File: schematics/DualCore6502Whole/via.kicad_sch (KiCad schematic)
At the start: 4 parts, among them J3 PORTA/PORTB, U15 W65C22N

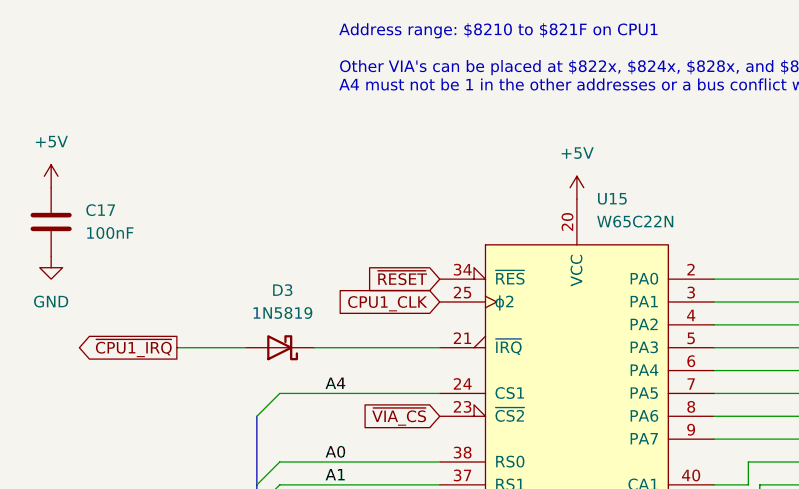
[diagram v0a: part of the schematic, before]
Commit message: Remove the need to multiplex the control lines
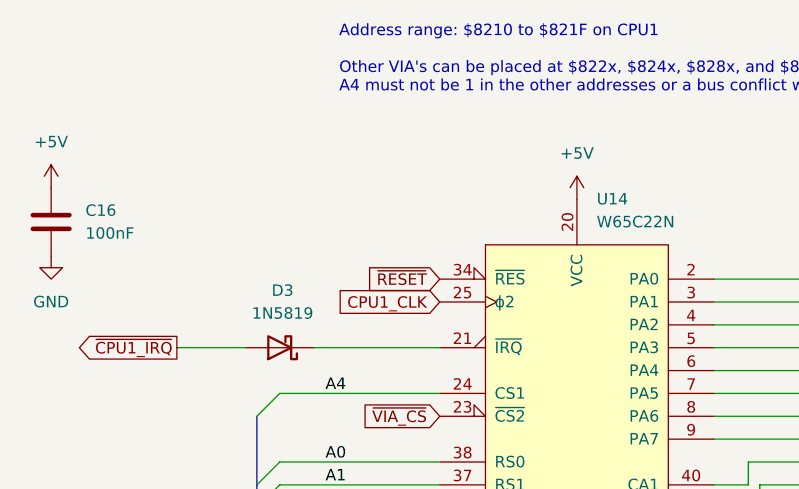
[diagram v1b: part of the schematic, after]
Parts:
- renumbered C17 to C16, U15 to U14
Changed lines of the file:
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@@
 		(dnp no)
 		(fields_autoplaced yes)
-		(property "Reference" "#PWR86"
+		(property "Reference" "#PWR79"
 			(at 78.74 59.69 0)
 			(effects
@@
 			(project "DualCore6502Whole"
 				(path "/93e0914e-b2e9-49c2-95f2-7cc419f4ea20/1a8142fa-4025-476a-8951-987d5052a061"
-					(reference "#PWR86")
+					(reference "#PWR79")
 					(unit 1)
 				)
@@
 		(dnp no)
 		(fields_autoplaced yes)
-		(property "Reference" "#PWR89"
+		(property "Reference" "#PWR82"
 			(at 137.16 137.16 0)
 			(effects
@@
 			(project ""
 				(path "/93e0914e-b2e9-49c2-95f2-7cc419f4ea20/1a8142fa-4025-476a-8951-987d5052a061"
-					(reference "#PWR89")
+					(reference "#PWR82")
 					(unit 1)
 				)
@@
 		(dnp no)
 		(fields_autoplaced yes)
-		(property "Reference" "#PWR88"
+		(property "Reference" "#PWR81"
 			(at 137.16 60.96 0)
 			(effects
@@
 			(project ""
 				(path "/93e0914e-b2e9-49c2-95f2-7cc419f4ea20/1a8142fa-4025-476a-8951-987d5052a061"
-					(reference "#PWR88")
+					(reference "#PWR81")
 					(unit 1)
 				)
@@
 		(dnp no)
 		(fields_autoplaced yes)
-		(property "Reference" "#PWR91"
+		(property "Reference" "#PWR84"
 			(at 165.1 93.98 0)
 			(effects
@@
 			(project "DualCore6502Whole"
 				(path "/93e0914e-b2e9-49c2-95f2-7cc419f4ea20/1a8142fa-4025-476a-8951-987d5052a061"
-					(reference "#PWR91")
+					(reference "#PWR84")
 					(unit 1)
 				)
@@
 		(dnp no)
 		(fields_autoplaced yes)
-		(property "Reference" "C17"
+		(property "Reference" "C16"
 			(at 82.55 58.42 0)
 			(effects
@@
 			(project "DualCore6502Whole"
 				(path "/93e0914e-b2e9-49c2-95f2-7cc419f4ea20/1a8142fa-4025-476a-8951-987d5052a061"
-					(reference "C17")
+					(reference "C16")
 					(unit 1)
 				)
@@
 		(dnp no)
 		(fields_autoplaced yes)
-		(property "Reference" "#PWR87"
+		(property "Reference" "#PWR80"
 			(at 78.74 69.85 0)
 			(effects
@@
 			(project "DualCore6502Whole"
 				(path "/93e0914e-b2e9-49c2-95f2-7cc419f4ea20/1a8142fa-4025-476a-8951-987d5052a061"
-					(reference "#PWR87")
+					(reference "#PWR80")
 					(unit 1)
 				)
@@
 		(dnp no)
 		(fields_autoplaced yes)
-		(property "Reference" "U15"
+		(property "Reference" "U14"
 			(at 139.3541 57.15 0)
 			(effects
@@
 			(project ""
 				(path "/93e0914e-b2e9-49c2-95f2-7cc419f4ea20/1a8142fa-4025-476a-8951-987d5052a061"
-					(reference "U15")
+					(reference "U14")
 					(unit 1)
 				)
@@
 		(dnp no)
 		(fields_autoplaced yes)
-		(property "Reference" "#PWR90"
+		(property "Reference" "#PWR83"
 			(at 175.26 91.44 0)
 			(effects
@@
 			(project "DualCore6502Whole"
 				(path "/93e0914e-b2e9-49c2-95f2-7cc419f4ea20/1a8142fa-4025-476a-8951-987d5052a061"
-					(reference "#PWR90")
-					(unit 1)
-				)
+					(reference "#PWR83")
+					(unit 1)
+				)

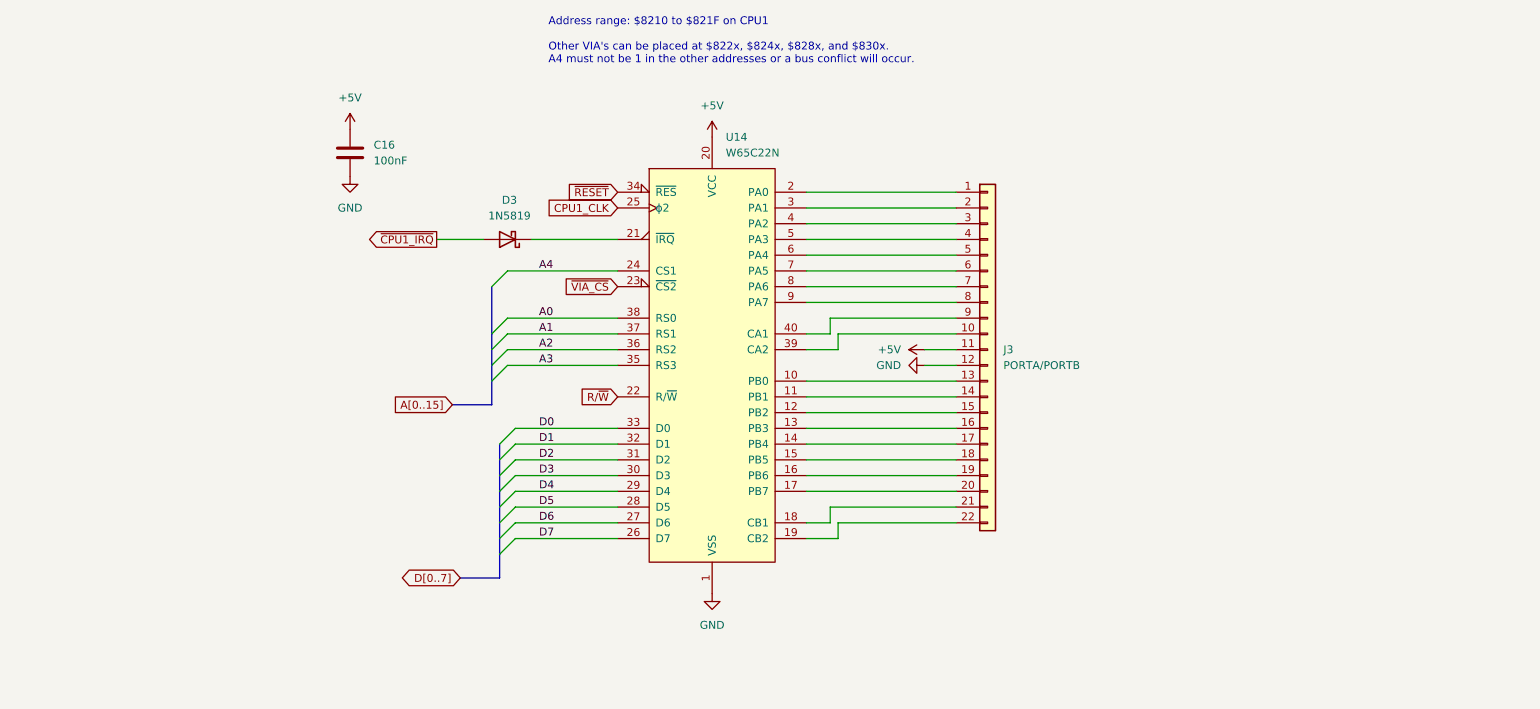
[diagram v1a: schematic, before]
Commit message: Add simpler I/O outputs as an alternative to the VIA
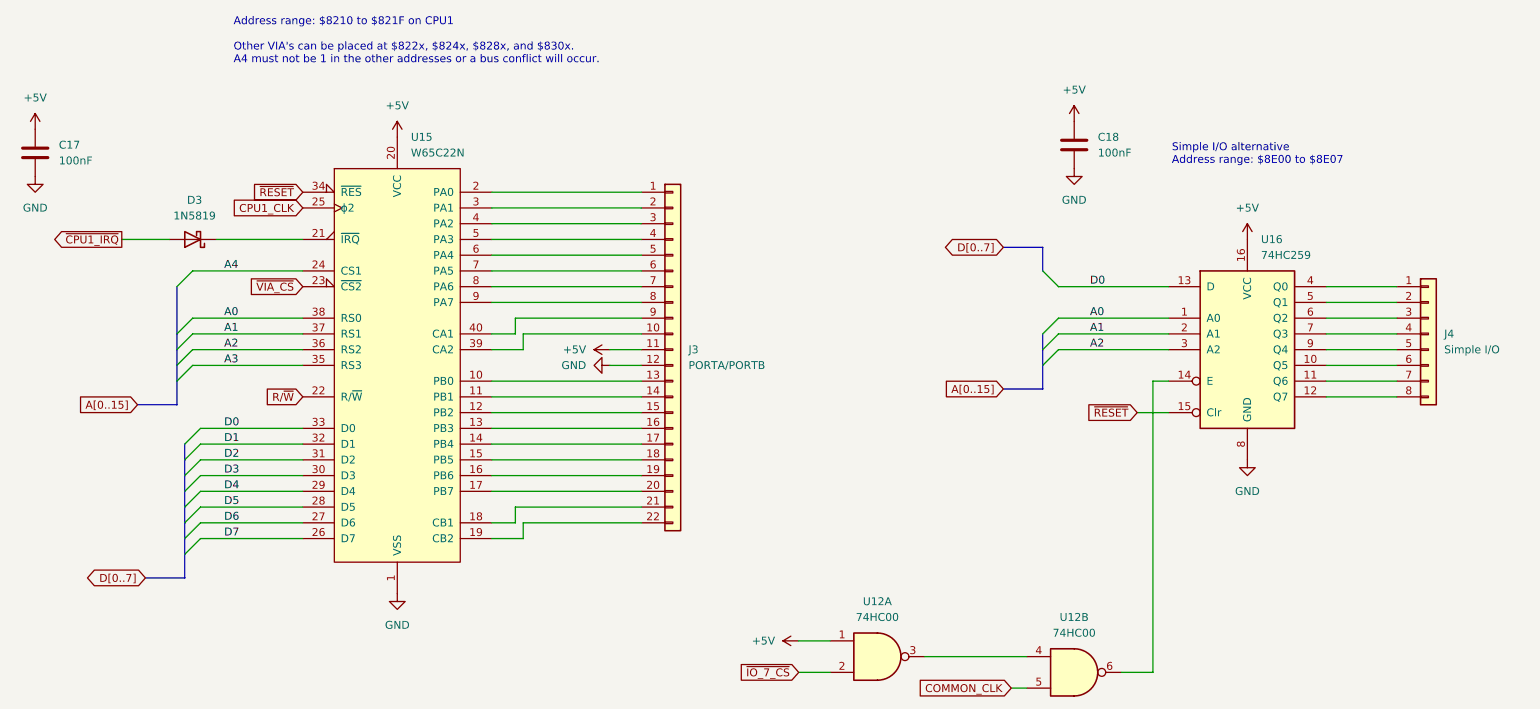
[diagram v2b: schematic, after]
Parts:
- added C18: 100nF, Capacitor_THT:C_Disc_D5.0mm_W2.5mm_P5.00mm, symbol Device:C
- added J4: Simple I/O, Connector_PinHeader_2.54mm:PinHeader_1x08_P2.54mm_Vertical, symbol Connector_Generic:Conn_01x08
- added U12: 74HC00, Package_DIP:DIP-14_W7.62mm, symbol 74xx:74LS00
- added U16: 74HC259, Package_DIP:DIP-16_W7.62mm, symbol 74xx:74LS259
- renumbered C16 to C17, U14 to U15
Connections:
- net +5V: now also C18.1, U12.1, U16.16 (VCC)
- net A0: now also U16.1 (A0)
- net A1: now also U16.2 (A1)
- net A2: now also U16.3 (A2)
- net D0: now also U16.13 (D)
- net GND: now also C18.2, U16.8 (GND)
- net ~{RESET}: now also U16.15 (Clr)
- new net: U12.3, U12.4
- new net: U12.6, U16.14 (E)
- new net: J4.6 (Pin_6), U16.10 (Q5)
- new net: J4.7 (Pin_7), U16.11 (Q6)
- new net: J4.8 (Pin_8), U16.12 (Q7)
- new net: J4.1 (Pin_1), U16.4 (Q0)
- new net: J4.2 (Pin_2), U16.5 (Q1)
- new net: J4.3 (Pin_3), U16.6 (Q2)
- new net: J4.4 (Pin_4), U16.7 (Q3)
- new net: J4.5 (Pin_5), U16.9 (Q4)
- new net COMMON_CLK: U12.5
- new net ~{IO_7_CS}: U12.2
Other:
- note added: "Simple I/O alternative Address range: $8E00 to $8E07"
- moved on the sheet: C17, D3, J3, U15

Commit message: Update the schematic
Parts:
- removed C18: 100nF, Capacitor_THT:C_Disc_D5.0mm_W2.5mm_P5.00mm, symbol Device:C
- removed J4: Simple I/O, Connector_PinHeader_2.54mm:PinHeader_1x08_P2.54mm_Vertical, symbol Connector_Generic:Conn_01x08
- removed U12: 74HC00, Package_DIP:DIP-14_W7.62mm, symbol 74xx:74LS00
- removed U16: 74HC259, Package_DIP:DIP-16_W7.62mm, symbol 74xx:74LS259
- added JP1: VIA IRQ, Connector_PinHeader_2.54mm:PinHeader_1x03_P2.54mm_Vertical, symbol Jumper:Jumper_3_Bridged12
- renumbered C17 to C21, D3 to D8, J3 to J4, U15 to U19
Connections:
- net CPU1_CLK is gone; now on net COMMON_CLK: U19.25 (ϕ2)
- net ~{CPU1_IRQ}: now also JP1.1 (A); no longer D8.2 (A)
- new net: D8.2 (A), JP1.2 (C)
- new net ~{CPU2_IRQ}: JP1.3 (B)
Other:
- note removed: "Simple I/O alternative Address range: $8E00 to $8E07"
- title: (none) -> Dual Core 65C02 Computer
- moved on the sheet: C21, D8, J4, U19

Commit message: Basic PCB layout
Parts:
- U18: renamed from U19; footprint Package_DIP:DIP-40_W15.24mm -> Package_DIP:DIP-40_W15.24mm_Socket
- renumbered C21 to C20, D8 to D7
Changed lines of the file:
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@@
 		(dnp no)
 		(fields_autoplaced yes)
-		(property "Reference" "#PWR116"
+		(property "Reference" "#PWR112"
 			(at 85.09 64.77 0)
 			(effects
@@
 			(project "DualCore6502Whole"
 				(path "/93e0914e-b2e9-49c2-95f2-7cc419f4ea20/1a8142fa-4025-476a-8951-987d5052a061"
-					(reference "#PWR116")
+					(reference "#PWR112")
 					(unit 1)
 				)
@@
 		(dnp no)
 		(fields_autoplaced yes)
-		(property "Reference" "#PWR119"
+		(property "Reference" "#PWR115"
 			(at 143.51 142.24 0)
 			(effects
@@
 			(project ""
 				(path "/93e0914e-b2e9-49c2-95f2-7cc419f4ea20/1a8142fa-4025-476a-8951-987d5052a061"
-					(reference "#PWR119")
+					(reference "#PWR115")
 					(unit 1)
 				)
@@
 		(dnp no)
 		(fields_autoplaced yes)
-		(property "Reference" "#PWR118"
+		(property "Reference" "#PWR114"
 			(at 143.51 66.04 0)
 			(effects
@@
 			(project ""
 				(path "/93e0914e-b2e9-49c2-95f2-7cc419f4ea20/1a8142fa-4025-476a-8951-987d5052a061"
-					(reference "#PWR118")
+					(reference "#PWR114")
 					(unit 1)
 				)
@@
 		(dnp no)
 		(fields_autoplaced yes)
-		(property "Reference" "D8"
+		(property "Reference" "D7"
 			(at 106.9975 72.39 0)
 			(effects
@@
 			(project "DualCore6502Whole"
 				(path "/93e0914e-b2e9-49c2-95f2-7cc419f4ea20/1a8142fa-4025-476a-8951-987d5052a061"
-					(reference "D8")
+					(reference "D7")
 					(unit 1)
 				)
@@
 		(dnp no)
 		(fields_autoplaced yes)
-		(property "Reference" "#PWR121"
+		(property "Reference" "#PWR117"
 			(at 171.45 99.06 0)
 			(effects
@@
 			(project "DualCore6502Whole"
 				(path "/93e0914e-b2e9-49c2-95f2-7cc419f4ea20/1a8142fa-4025-476a-8951-987d5052a061"
-					(reference "#PWR121")
+					(reference "#PWR117")
 					(unit 1)
 				)
@@
 		(dnp no)
 		(fields_autoplaced yes)
-		(property "Reference" "C21"
+		(property "Reference" "C20"
 			(at 88.9 63.5 0)
 			(effects
@@
 			(project "DualCore6502Whole"
 				(path "/93e0914e-b2e9-49c2-95f2-7cc419f4ea20/1a8142fa-4025-476a-8951-987d5052a061"
-					(reference "C21")
+					(reference "C20")
 					(unit 1)
 				)
@@
 		(dnp no)
 		(fields_autoplaced yes)
-		(property "Reference" "#PWR117"
+		(property "Reference" "#PWR113"
 			(at 85.09 74.93 0)
 			(effects
@@
 			(project "DualCore6502Whole"
 				(path "/93e0914e-b2e9-49c2-95f2-7cc419f4ea20/1a8142fa-4025-476a-8951-987d5052a061"
-					(reference "#PWR117")
+					(reference "#PWR113")
 					(unit 1)
 				)
@@
 		(dnp no)
 		(fields_autoplaced yes)
-		(property "Reference" "U19"
+		(property "Reference" "U18"
 			(at 145.7041 62.23 0)
 			(effects
@@
 			)
 		)
-		(property "Footprint" "Package_DIP:DIP-40_W15.24mm"
+		(property "Footprint" "Package_DIP:DIP-40_W15.24mm_Socket"
 			(at 143.51 95.25 0)
 			(effects
@@
 			(project ""
 				(path "/93e0914e-b2e9-49c2-95f2-7cc419f4ea20/1a8142fa-4025-476a-8951-987d5052a061"
-					(reference "U19")
+					(reference "U18")
 					(unit 1)
 				)
@@
 		(dnp no)
 		(fields_autoplaced yes)
-		(property "Reference" "#PWR120"
+		(property "Reference" "#PWR116"
 			(at 181.61 96.52 0)
 			(effects
@@
 			(project "DualCore6502Whole"
 				(path "/93e0914e-b2e9-49c2-95f2-7cc419f4ea20/1a8142fa-4025-476a-8951-987d5052a061"
-					(reference "#PWR120")
-					(unit 1)
-				)
+					(reference "#PWR116")
+					(unit 1)
+				)
